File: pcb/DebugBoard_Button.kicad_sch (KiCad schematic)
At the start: 2 parts, among them SW2 B3U-1000P

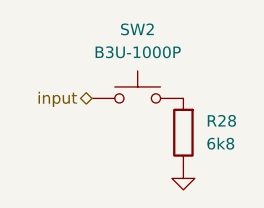
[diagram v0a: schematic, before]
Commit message: Made `DebugBoard` target and fixed some GPIO discrepancies.
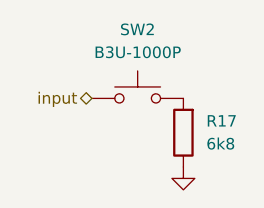
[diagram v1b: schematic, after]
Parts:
- renumbered R28 to R17
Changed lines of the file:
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@@
 		(dnp no)
 		(fields_autoplaced yes)
-		(property "Reference" "#PWR017"
+		(property "Reference" "#PWR034"
 			(at 105.41 85.09 0)
 			(effects
@@
 			(project "DebugBoard"
 				(path "/5ece3d0a-e9bb-4e6a-946b-805aaca75ace/9b25b03f-30dc-49f9-97ea-7f1a5be5a1ae"
-					(reference "#PWR018")
+					(reference "#PWR035")
 					(unit 1)
 				)
 				(path "/5ece3d0a-e9bb-4e6a-946b-805aaca75ace/9f8da623-da6a-4a3e-905a-06dca0b6f272"
-					(reference "#PWR017")
+					(reference "#PWR034")
 					(unit 1)
 				)
@@
 		(on_board yes)
 		(dnp no)
-		(property "Reference" "R28"
+		(property "Reference" "R17"
 			(at 107.95 73.6599 0)
 			(effects
@@
 			(project "DebugBoard"
 				(path "/5ece3d0a-e9bb-4e6a-946b-805aaca75ace/9b25b03f-30dc-49f9-97ea-7f1a5be5a1ae"
-					(reference "R29")
+					(reference "R18")
 					(unit 1)
 				)
 				(path "/5ece3d0a-e9bb-4e6a-946b-805aaca75ace/9f8da623-da6a-4a3e-905a-06dca0b6f272"
-					(reference "R28")
+					(reference "R17")
 					(unit 1)
 				)
@@
 			(project "DebugBoard"
 				(path "/5ece3d0a-e9bb-4e6a-946b-805aaca75ace/9b25b03f-30dc-49f9-97ea-7f1a5be5a1ae"
-					(reference "SW1")
+					(reference "SW3")
 					(unit 1)
 				)

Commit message: Placed silkscreen for `DebugBoard`.
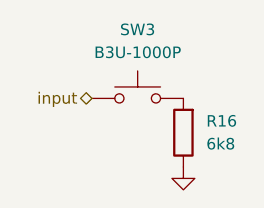
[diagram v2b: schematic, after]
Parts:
- renumbered R17 to R16, SW2 to SW3
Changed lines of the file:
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@@
 		(on_board yes)
 		(dnp no)
-		(property "Reference" "R17"
+		(property "Reference" "R16"
 			(at 107.95 73.6599 0)
 			(effects
@@
 			(project "DebugBoard"
 				(path "/5ece3d0a-e9bb-4e6a-946b-805aaca75ace/9b25b03f-30dc-49f9-97ea-7f1a5be5a1ae"
-					(reference "R18")
+					(reference "R15")
 					(unit 1)
 				)
 				(path "/5ece3d0a-e9bb-4e6a-946b-805aaca75ace/9f8da623-da6a-4a3e-905a-06dca0b6f272"
-					(reference "R17")
+					(reference "R16")
 					(unit 1)
 				)
@@
 		(dnp no)
 		(fields_autoplaced yes)
-		(property "Reference" "SW2"
+		(property "Reference" "SW3"
 			(at 100.33 63.5 0)
 			(effects
@@
 			(project "DebugBoard"
 				(path "/5ece3d0a-e9bb-4e6a-946b-805aaca75ace/9b25b03f-30dc-49f9-97ea-7f1a5be5a1ae"
+					(reference "SW4")
+					(unit 1)
+				)
+				(path "/5ece3d0a-e9bb-4e6a-946b-805aaca75ace/9f8da623-da6a-4a3e-905a-06dca0b6f272"
 					(reference "SW3")
 					(unit 1)
 				)
-				(path "/5ece3d0a-e9bb-4e6a-946b-805aaca75ace/9f8da623-da6a-4a3e-905a-06dca0b6f272"
-					(reference "SW2")
-					(unit 1)
-				)
